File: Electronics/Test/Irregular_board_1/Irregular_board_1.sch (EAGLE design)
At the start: 9 parts

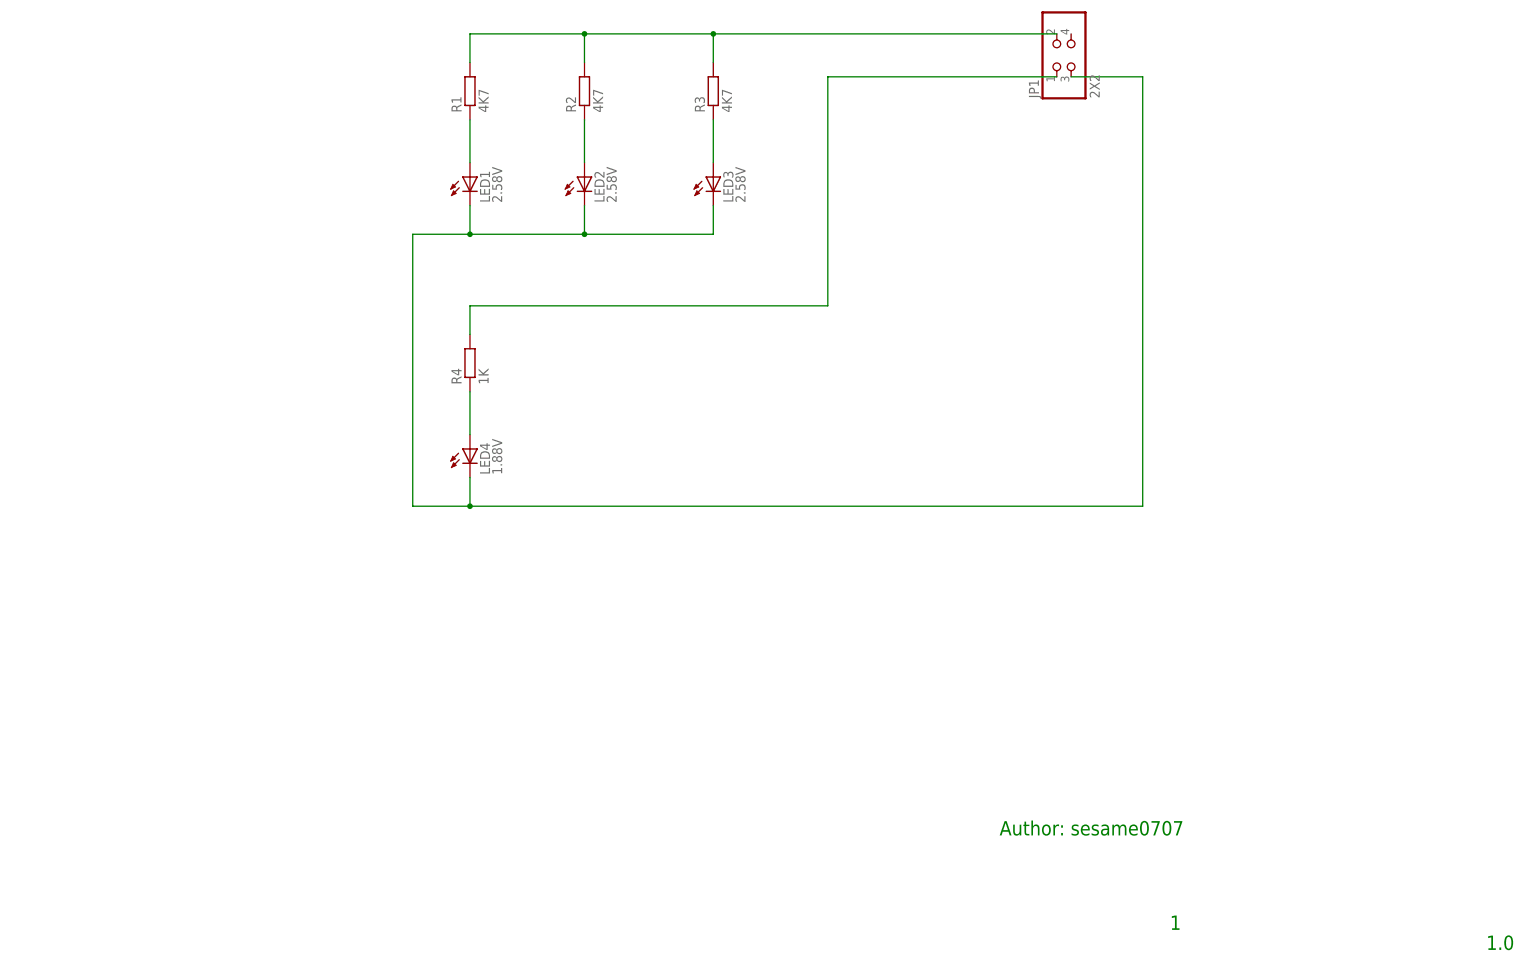
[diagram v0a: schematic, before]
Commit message: List of parts updated
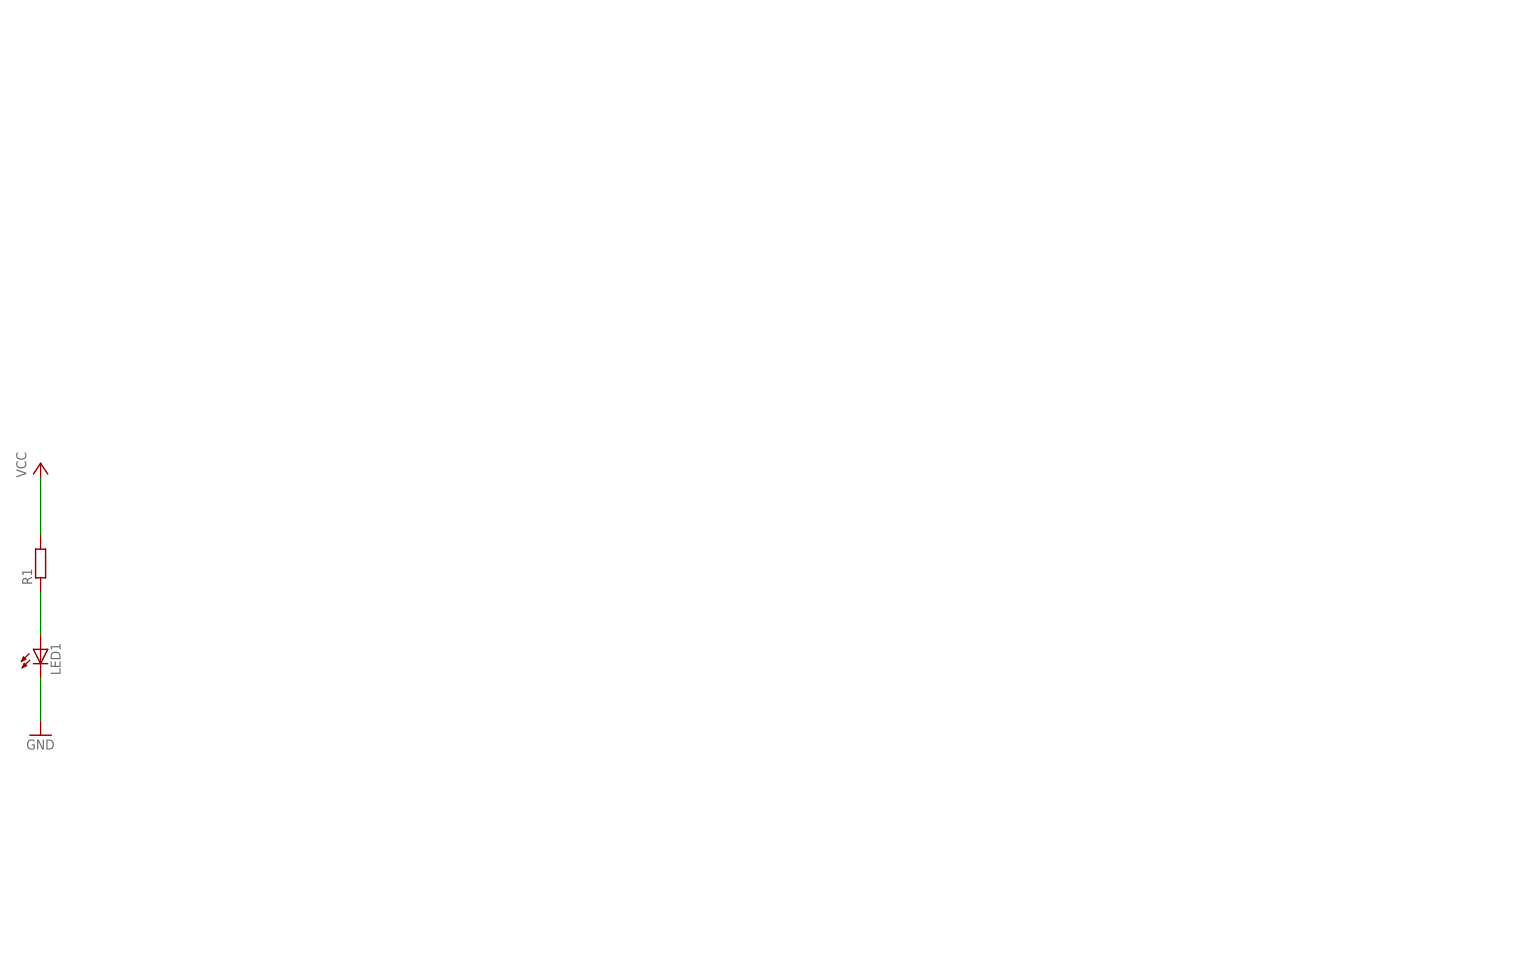
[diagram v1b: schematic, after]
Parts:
- removed JP1: 2X2, pinhead:PINHD-2X2
- removed LED2, LED3: 2.58V, led:LED5MM
- removed LED4: 1.88V, led:LED5MM
- removed R2, R3: 4K7, resistor:R-EU_0204/2V
- removed R4: 1K, resistor:R-EU_0204/2V
- LED1: value 2.58V -> (none)
- R1: value 4K7 -> (none); device resistor:R-EU_0204/2V -> rcl:R-EU_0204/2V
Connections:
- removed net N$2: LED2.A, R2.1
- removed net N$3: LED3.A, R3.1
- removed net N$4: LED4.A, R4.1
- removed net N$5: JP1.2, R1.2, R2.2, R3.2
- removed net N$6: JP1.1, R4.2
- removed net N$7: JP1.3, LED1.C, LED2.C, LED3.C, LED4.C
- new net GND: LED1.C
- new net VCC: R1.2
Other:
- note removed: "1"
- note removed: "1.0"
- note removed: "Author: sesame0707"
- moved on the sheet: LED1, R1
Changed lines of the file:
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@@
 <grid distance="0.1" unitdist="inch" unit="inch" style="lines" multiple="1" display="no" altdistance="0.01" altunitdist="inch" altunit="inch"/>
 <layers>
-<layer number="1" name="Top" color="4" fill="1" visible="no" active="no"/>
+<layer number="1" name="Top" color="4" fill="10" visible="no" active="no"/>
 <layer number="16" name="Bottom" color="1" fill="1" visible="no" active="no"/>
 <layer number="17" name="Pads" color="2" fill="1" visible="no" active="no"/>
@@
 <layer number="19" name="Unrouted" color="6" fill="1" visible="no" active="no"/>
 <layer number="20" name="Dimension" color="15" fill="1" visible="no" active="no"/>
-<layer number="21" name="tPlace" color="7" fill="1" visible="no" active="no"/>
+<layer number="21" name="tPlace" color="7" fill="9" visible="no" active="no"/>
 <layer number="22" name="bPlace" color="7" fill="1" visible="no" active="no"/>
-<layer number="23" name="tOrigins" color="15" fill="1" visible="no" active="no"/>
+<layer number="23" name="tOrigins" color="7" fill="1" visible="no" active="no"/>
 <layer number="24" name="bOrigins" color="15" fill="1" visible="no" active="no"/>
 <layer number="25" name="tNames" color="7" fill="1" visible="no" active="no"/>
@@
 <layer number="45" name="Holes" color="7" fill="1" visible="no" active="no"/>
 <layer number="46" name="Milling" color="3" fill="1" visible="no" active="no"/>
-<layer number="47" name="Measures" color="7" fill="1" visible="no" active="no"/>
+<layer number="47" name="Measures" color="5" fill="1" visible="no" active="no"/>
 <layer number="48" name="Document" color="7" fill="1" visible="no" active="no"/>
 <layer number="49" name="Reference" color="7" fill="1" visible="no" active="no"/>
-<layer number="51" name="tDocu" color="7" fill="1" visible="no" active="no"/>
+<layer number="51" name="tDocu" color="6" fill="9" visible="no" active="no"/>
 <layer number="52" name="bDocu" color="7" fill="1" visible="no" active="no"/>
 <layer number="90" name="Modules" color="5" fill="1" visible="yes" active="yes"/>
@@
 <layer number="97" name="Info" color="7" fill="1" visible="yes" active="yes"/>
 <layer number="98" name="Guide" color="6" fill="1" visible="yes" active="yes"/>
-<layer number="99" name="SpiceOrder" color="5" fill="1" visible="yes" active="yes"/>
 </layers>
 <schematic xreflabel="%F%N/%S.%C%R" xrefpart="/%S.%C%R">
@@
 </classes>
 <parts>
-<part name="FRAME1" library="frames" deviceset="FRAME_A_L" device="" value="Main"/>
-<part name="LED1" library="led" deviceset="LED" device="5MM" value="2.58V"/>
-<part name="LED2" library="led" deviceset="LED" device="5MM" value="2.58V"/>
-<part name="LED3" library="led" deviceset="LED" device="5MM" value="2.58V"/>
-<part name="LED4" library="led" deviceset="LED" device="5MM" value="1.88V"/>
-<part name="R1" library="resistor" deviceset="R-EU_" device="0204/2V" value="4K7"/>
-<part name="R2" library="resistor" deviceset="R-EU_" device="0204/2V" value="4K7"/>
-<part name="R3" library="resistor" deviceset="R-EU_" device="0204/2V" value="4K7"/>
-<part name="R4" library="resistor" deviceset="R-EU_" device="0204/2V" value="1K"/>
-<part name="JP1" library="pinhead" deviceset="PINHD-2X2" device="" value="2X2"/>
+<part name="LED1" library="led" deviceset="LED" device="5MM"/>
+<part name="R1" library="rcl" deviceset="R-EU_" device="0204/2V"/>
+<part name="P+1" library="supply1" deviceset="VCC" device=""/>
+<part name="GND1" library="supply1" deviceset="GND" device=""/>
 </parts>
 <sheets>
 <sheet>
 <plain>
-<text x="261.62" y="7.62" size="2.54" layer="91">1.0</text>
-<text x="205.486" y="11.176" size="2.54" layer="91">1</text>
-<text x="175.26" y="27.94" size="2.54" layer="91">Author: sesame0707</text>
 </plain>
 <instances>
-<instance part="FRAME1" gate="G$1" x="0" y="0"/>
-<instance part="FRAME1" gate="G$2" x="172.72" y="0"/>
-<instance part="LED1" gate="G$1" x="81.28" y="144.78"/>
-<instance part="LED2" gate="G$1" x="101.6" y="144.78"/>
-<instance part="LED3" gate="G$1" x="124.46" y="144.78"/>
-<instance part="LED4" gate="G$1" x="81.28" y="96.52"/>
-<instance part="R1" gate="G$1" x="81.28" y="160.02" rot="R90"/>
-<instance part="R2" gate="G$1" x="101.6" y="160.02" rot="R90"/>
-<instance part="R3" gate="G$1" x="124.46" y="160.02" rot="R90"/>
-<instance part="R4" gate="G$1" x="81.28" y="111.76" rot="R90"/>
-<instance part="JP1" gate="A" x="187.96" y="167.64" rot="R90"/>
+<instance part="LED1" gate="G$1" x="5.08" y="60.96"/>
+<instance part="R1" gate="G$1" x="5.08" y="76.2" rot="R90"/>
+<instance part="P+1" gate="VCC" x="5.08" y="93.98"/>
+<instance part="GND1" gate="1" x="5.08" y="45.72"/>
 </instances>
 <busses>
 </busses>
 <nets>
+<net name="VCC" class="0">
+<segment>
+<pinref part="P+1" gate="VCC" pin="VCC"/>
+<pinref part="R1" gate="G$1" pin="2"/>
+<wire x1="5.08" y1="91.44" x2="5.08" y2="81.28" width="0.1524" layer="91"/>
+</segment>
+</net>
 <net name="N$1" class="0">
 <segment>
 <pinref part="R1" gate="G$1" pin="1"/>
 <pinref part="LED1" gate="G$1" pin="A"/>
-<wire x1="81.28" y1="154.94" x2="81.28" y2="147.32" width="0.1524" layer="91"/>
+<wire x1="5.08" y1="71.12" x2="5.08" y2="63.5" width="0.1524" layer="91"/>
 </segment>
 </net>
-<net name="N$2" class="0">
+<net name="GND" class="0">
 <segment>
-<pinref part="R2" gate="G$1" pin="1"/>
-<pinref part="LED2" gate="G$1" pin="A"/>
-<wire x1="101.6" y1="154.94" x2="101.6" y2="147.32" width="0.1524" layer="91"/>
+<pinref part="LED1" gate="G$1" pin="C"/>
+<pinref part="GND1" gate="1" pin="GND"/>
+<wire x1="5.08" y1="55.88" x2="5.08" y2="48.26" width="0.1524" layer="91"/>
 </segment>
 </net>
-<net name="N$3" class="0">
-<segment>
-<pinref part="R3" gate="G$1" pin="1"/>
-<pinref part="LED3" gate="G$1" pin="A"/>
-<wire x1="124.46" y1="154.94" x2="124.46" y2="147.32" width="0.1524" layer="91"/>
-</segment>
-</net>
-<net name="N$4" class="0">
-<segment>
-<pinref part="R4" gate="G$1" pin="1"/>
-<pinref part="LED4" gate="G$1" pin="A"/>
-<wire x1="81.28" y1="106.68" x2="81.28" y2="99.06" width="0.1524" layer="91"/>
-</segment>
-</net>
-<net name="N$5" class="0">
-<segment>
-<pinref part="R1" gate="G$1" pin="2"/>
-<wire x1="81.28" y1="165.1" x2="81.28" y2="170.18" width="0.1524" layer="91"/>
-<wire x1="81.28" y1="170.18" x2="101.6" y2="170.18" width="0.1524" layer="91"/>
-<pinref part="R2" gate="G$1" pin="2"/>
-<wire x1="101.6" y1="170.18" x2="124.46" y2="170.18" width="0.1524" layer="91"/>
-<wire x1="124.46" y1="170.18" x2="185.42" y2="170.18" width="0.1524" layer="91"/>
-<wire x1="101.6" y1="165.1" x2="101.6" y2="170.18" width="0.1524" layer="91"/>
-<junction x="101.6" y="170.18"/>
-<pinref part="R3" gate="G$1" pin="2"/>
-<wire x1="124.46" y1="165.1" x2="124.46" y2="170.18" width="0.1524" layer="91"/>
-<junction x="124.46" y="170.18"/>
-<pinref part="JP1" gate="A" pin="2"/>
-</segment>
-</net>
-<net name="N$6" class="0">
-<segment>
-<pinref part="R4" gate="G$1" pin="2"/>
-<wire x1="81.28" y1="116.84" x2="81.28" y2="121.92" width="0.1524" layer="91"/>
-<wire x1="81.28" y1="121.92" x2="144.78" y2="121.92" width="0.1524" layer="91"/>
-<wire x1="144.78" y1="121.92" x2="144.78" y2="162.56" width="0.1524" layer="91"/>
-<pinref part="JP1" gate="A" pin="1"/>
-<wire x1="144.78" y1="162.56" x2="185.42" y2="162.56" width="0.1524" layer="91"/>
-</segment>
-</net>
-<net name="N$7" class="0">
-<segment>
-<pinref part="LED1" gate="G$1" pin="C"/>
-<wire x1="81.28" y1="139.7" x2="81.28" y2="134.62" width="0.1524" layer="91"/>
-<wire x1="81.28" y1="134.62" x2="71.12" y2="134.62" width="0.1524" layer="91"/>
-<wire x1="71.12" y1="134.62" x2="71.12" y2="86.36" width="0.1524" layer="91"/>
-<wire x1="71.12" y1="86.36" x2="81.28" y2="86.36" width="0.1524" layer="91"/>
-<wire x1="81.28" y1="86.36" x2="200.66" y2="86.36" width="0.1524" layer="91"/>
-<wire x1="200.66" y1="86.36" x2="200.66" y2="162.56" width="0.1524" layer="91"/>
-<pinref part="JP1" gate="A" pin="3"/>
-<wire x1="200.66" y1="162.56" x2="187.96" y2="162.56" width="0.1524" layer="91"/>
-<wire x1="81.28" y1="134.62" x2="101.6" y2="134.62" width="0.1524" layer="91"/>
-<junction x="81.28" y="134.62"/>
-<pinref part="LED3" gate="G$1" pin="C"/>
-<wire x1="101.6" y1="134.62" x2="124.46" y2="134.62" width="0.1524" layer="91"/>
-<wire x1="124.46" y1="134.62" x2="124.46" y2="139.7" width="0.1524" layer="91"/>
-<pinref part="LED2" gate="G$1" pin="C"/>
-<wire x1="101.6" y1="139.7" x2="101.6" y2="134.62" width="0.1524" layer="91"/>
-<junction x="101.6" y="134.62"/>
-<pinref part="LED4" gate="G$1" pin="C"/>
-<wire x1="81.28" y1="91.44" x2="81.28" y2="86.36" width="0.1524" layer="91"/>
-<junction x="81.28" y="86.36"/>
-</segment>
-</net>
